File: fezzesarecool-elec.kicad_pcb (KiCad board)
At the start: 2 copper layers, 91 parts, among them J1 Conn_sel, J10 SWD-6, J11 SWD-7, J12 SWD-8, J13 Conn_reset, J14 Conn_LEDs, J15 Audio_input, J16 alim_rpi, J17 alim_audio, J18 alim_led, J2 Conn_start, J3 CAN_conn, J4 CAN_conn, J5 SWD-1, J6 SWD-2, J7 SWD-3, J8 SWD-4, J9 SWD-5, P1 Conn_02x20_Odd_Even, Q1 NMOS-T252, Q2 NMOS-T252, Q3 NMOS-T252, Q4 BSS138, Q5 BSS138, U1 MCP2515-EST, U10 SN74LVC1G00, U11 MC34152, U12 MC34152, U13 LM4991, U2 MCP2551-I-SN, U3 SN74CB3Q3257, U4 SN74CB3Q3257, U5 SN74AC08, U6 SN74CB3Q3257, U7 SN74AC08, U8 SN74CB3Q3257, U9 SN74CB3Q3257, Y1 Crystal_8MHz

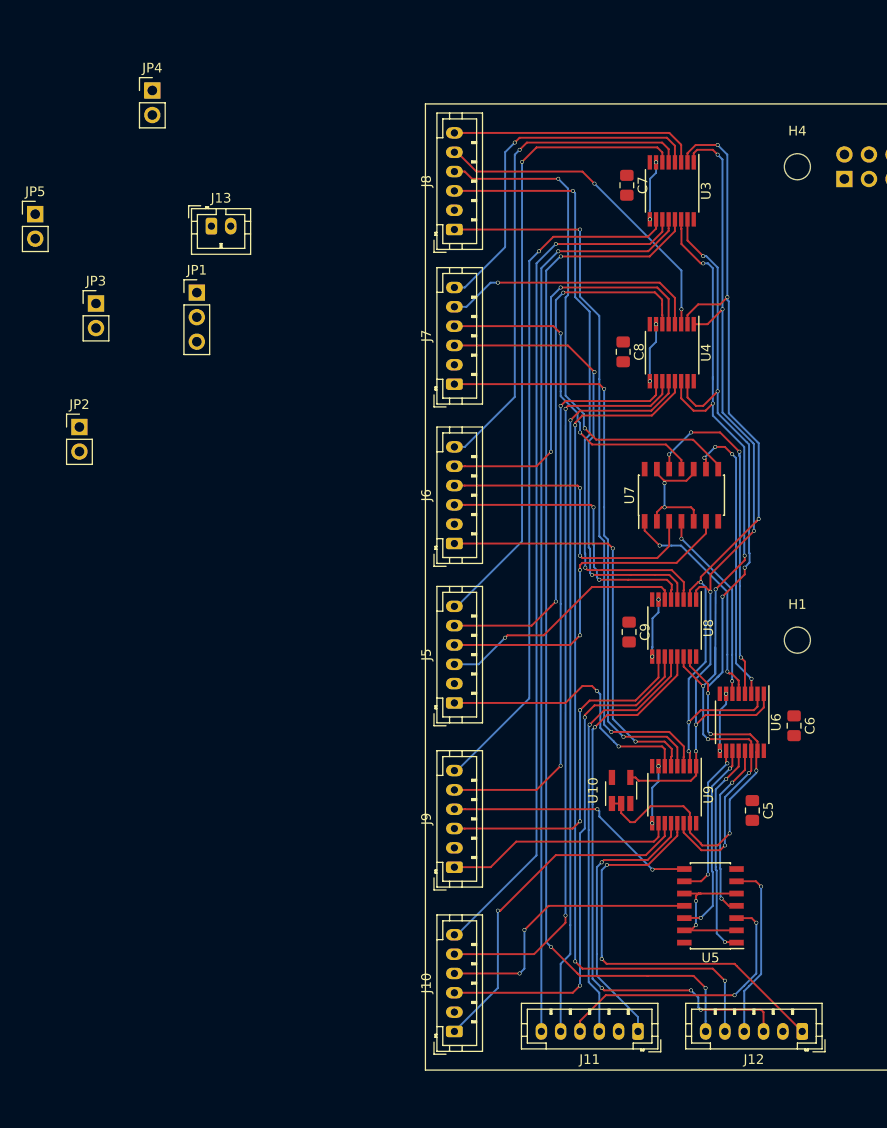
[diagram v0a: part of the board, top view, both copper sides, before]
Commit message: multiplexeur moved
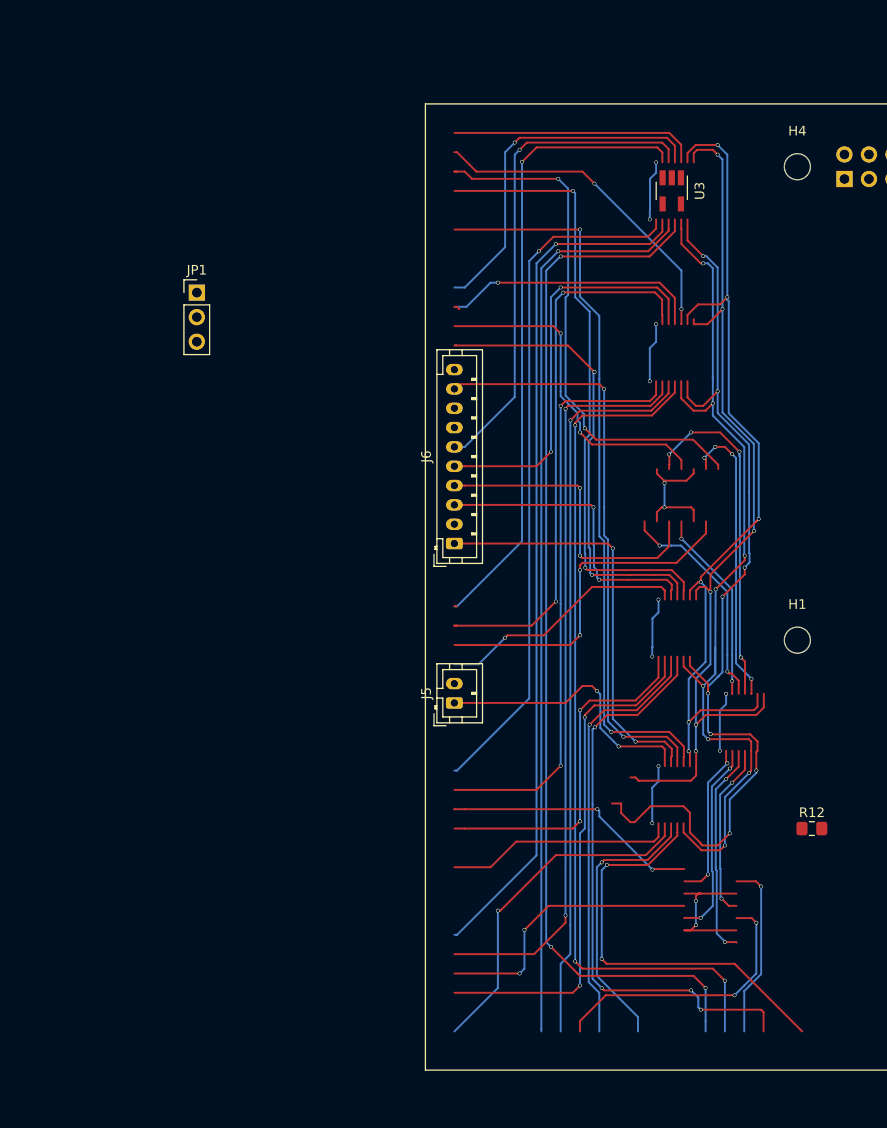
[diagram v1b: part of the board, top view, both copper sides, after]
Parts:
- removed C5, C6, C7, C8, C9: C, Capacitor_SMD:C_0805_2012Metric_Pad1.15x1.40mm_HandSolder
- removed J10: SWD-6, Connector_JST:JST_PH_B6B-PH-K_1x06_P2.00mm_Vertical
- removed J11: SWD-7, Connector_JST:JST_PH_B6B-PH-K_1x06_P2.00mm_Vertical
- removed J12: SWD-8, Connector_JST:JST_PH_B6B-PH-K_1x06_P2.00mm_Vertical
- removed J13: Conn_reset, Connector_JST:JST_PH_B2B-PH-K_1x02_P2.00mm_Vertical
- removed J7: SWD-3, Connector_JST:JST_PH_B6B-PH-K_1x06_P2.00mm_Vertical
- removed J8: SWD-4, Connector_JST:JST_PH_B6B-PH-K_1x06_P2.00mm_Vertical
- removed J9: SWD-5, Connector_JST:JST_PH_B6B-PH-K_1x06_P2.00mm_Vertical
- removed JP2: Jumper_RX, Connector_PinHeader_2.54mm:PinHeader_1x02_P2.54mm_Vertical
- removed JP3: Jumper_TX, Connector_PinHeader_2.54mm:PinHeader_1x02_P2.54mm_Vertical
- removed JP4: Jumper_SWDIO, Connector_PinHeader_2.54mm:PinHeader_1x02_P2.54mm_Vertical
- removed JP5: Jumper_SWCLK, Connector_PinHeader_2.54mm:PinHeader_1x02_P2.54mm_Vertical
- removed U10: SN74LVC1G00, Package_TO_SOT_SMD:SOT-23-5_HandSoldering
- removed U4, U6, U8, U9: SN74CB3Q3257, Package_SO:TSSOP-16_4.4x5mm_P0.65mm
- removed U5, U7: SN74AC08, Package_SO:SOIC-14_3.9x8.7mm_P1.27mm
- added R12: R, Resistor_SMD:R_0805_2012Metric_Pad1.15x1.40mm_HandSolder, F.Cu at (205.0, 166.0)
- J5: value SWD-1 -> Conn_01x02; footprint Connector_JST:JST_PH_B6B-PH-K_1x06_P2.00mm_Vertical -> Connector_JST:JST_PH_B2B-PH-K_1x02_P2.00mm_Vertical
- J6: value SWD-2 -> Conn_01x10; footprint Connector_JST:JST_PH_B6B-PH-K_1x06_P2.00mm_Vertical -> Connector_JST:JST_PH_B10B-PH-K_1x10_P2.00mm_Vertical
- U3: value SN74CB3Q3257 -> SN74AHC1G08; footprint Package_SO:TSSOP-16_4.4x5mm_P0.65mm -> Package_TO_SOT_SMD:SOT-23-5_HandSoldering
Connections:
- J5 pad 1: Net-(J5-Pad1) -> /SWD/GRST
- J6 pad 1: Net-(J6-Pad1) -> +3V3
- J6 pad 2: GND -> Net-(J6-Pad2)
- J6 pad 3: Net-(J6-Pad3) -> /GPIO24(GEN5)
- J6 pad 4: Net-(J6-Pad4) -> /GPIO25(GEN6)
- J6 pad 5: Net-(J6-Pad5) -> /GPIO15(RXD0)
- J6 pad 6: Net-(J6-Pad6) -> /GPIO14(TXD0)
- U3 pad 1: /SWD/~s2 -> /SWD/GRST
- U3 pad 2: /GPIO27(GEN2) -> /SWD/nrst
- U3 pad 3: Net-(J8-Pad6) -> GND
- U3 pad 4: Net-(J7-Pad6) -> Net-(J6-Pad2)
- U3 pad 5: Net-(J6-Pad6) -> +3V3
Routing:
- net Net-(J7-Pad1): track 60.5 -> 0.00 mm, vias 2 -> 0
- net /GPIO22(GEN3): track 102.2 -> 162.7 mm, vias 8 -> 10
- net Net-(J6-Pad6): track 51.8 -> 0.00 mm, vias 1 -> 0
- net /GPIO14(TXD0): track 0.00 -> 51.8 mm, vias 0 -> 1
- net Net-(J6-Pad1): track 43.5 -> 0.00 mm, vias 2 -> 0
- net +3V3: track 0.00 -> 43.5 mm, vias 0 -> 2
- net Net-(J6-Pad5): track 42.6 -> 0.00 mm, vias 2 -> 0
- net /GPIO15(RXD0): track 0.00 -> 42.6 mm, vias 0 -> 2
- net Net-(J6-Pad4): track 32.5 -> 0.00 mm, vias 2 -> 0
- net /GPIO25(GEN6): track 0.00 -> 32.5 mm, vias 0 -> 2
- net Net-(J6-Pad3): track 31.5 -> 0.00 mm, vias 2 -> 0
- net /GPIO24(GEN5): track 0.00 -> 31.5 mm, vias 0 -> 2
- net Net-(J5-Pad1): track 29.0 -> 0.00 mm, vias 2 -> 0
- net /SWD/GRST: track 30.2 -> 59.2 mm, vias 4 -> 6

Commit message: check rpi connexions
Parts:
- removed D3: LED, LED_SMD:LED_0805_2012Metric_Pad1.15x1.40mm_HandSolder
- removed D5: D, Diode_SMD:D_2114_3652Metric_Pad1.85x3.75mm_HandSolder
- removed F2: Fuse, Fuse:Fuse_1206_3216Metric_Pad1.42x1.75mm_HandSolder
- removed J16: alim_rpi, Connector_Phoenix_MSTB:PhoenixContact_MSTBA_2,5_2-G_1x02_P5.00mm_Horizontal
- removed J17: alim_audio, Connector_Phoenix_MSTB:PhoenixContact_MSTBA_2,5_2-G_1x02_P5.00mm_Horizontal
- removed JP6: Jumper_NC_Dual, Jumper:SolderJumper-3_P1.3mm_Open_RoundedPad1.0x1.5mm_NumberLabels
- removed R14, R15: R, Resistor_SMD:R_0805_2012Metric_Pad1.15x1.40mm_HandSolder
- added J7: alim_5V, Connector_Phoenix_MSTB:PhoenixContact_MSTBA_2,5_2-G_1x02_P5.00mm_Horizontal, F.Cu at (224.0, 141.0)
- added R13: R, Resistor_SMD:R_0805_2012Metric_Pad1.15x1.40mm_HandSolder, B.Cu at (222.5, 137.5)
- C14, D6, F3, R10, R11, R12, R16, U13, U3: moved to B.Cu
- J18: value alim_led -> alim_jacky
- J3, J4: footprint Connector_JST:JST_XH_B04B-XH-A_1x04_P2.50mm_Vertical -> Connector_JST:JST_XH_B05B-XH-A_1x05_P2.50mm_Vertical
- moved R16 159.1 mm to (205.0, 138.5), turned to 90 degrees
- moved D4 150.7 mm to (202.5, 138.5), turned to 90 degrees
- moved D6 144.0 mm to (213.5, 146.0)
- moved F3 136.0 mm to (207.5, 141.5), turned to 270 degrees
- moved J18 133.5 mm to (211.0, 141.0)
- moved JP7 127.1 mm to (209.7, 136.0)
- moved J2 122.0 mm to (253.4, 104.9)
- moved J1 122.0 mm to (245.5, 104.9)
- moved F1 111.5 mm to (221.0, 141.5), turned to 270 degrees
- moved D2 110.8 mm to (224.5, 146.5), turned to 0 degrees
- moved D1 108.0 mm to (217.5, 137.0), turned to 0 degrees
- moved R1 103.7 mm to (246.5, 110.0)
- moved R2 93.8 mm to (252.0, 110.0), turned to 180 degrees
- moved LS1 87.9 mm to (229.5, 129.0)
- moved JP1 83.7 mm to (224.0, 123.5), turned to 90 degrees
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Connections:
- C16 pad 1: +5VL -> +5VD
- J3 pad 3: Net-(J3-Pad3) -> /SWD/GRST
- J3 pad 4: +7.5V -> Net-(J3-Pad4)
- J4 pad 3: Net-(J3-Pad3) -> /SWD/GRST
- J4 pad 4: +7.5V -> Net-(J3-Pad4)
- U13 pad 6: +5VL -> +5VD
- U2 pad 7: Net-(J3-Pad3) -> Net-(J3-Pad4)
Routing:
- net /GPIO22(GEN3): track 162.7 -> 0.00 mm, vias 10 -> 0
- net Net-(J12-Pad6): track 108.7 -> 0.00 mm, vias 3 -> 0
- net /SWD/~s2: track 95.4 -> 0.00 mm, vias 6 -> 0
- net Net-(J11-Pad6): track 95.0 -> 0.00 mm, vias 1 -> 0
- net /GPIO17(GEN0): track 94.4 -> 0.00 mm, vias 8 -> 0
- net /GPIO27(GEN2): track 91.3 -> 0.00 mm, vias 6 -> 0
- net Net-(J12-Pad5): track 90.1 -> 0.00 mm, vias 3 -> 0
- net Net-(J10-Pad6): track 88.8 -> 0.00 mm, vias 1 -> 0
- net Net-(J10-Pad5): track 78.1 -> 0.00 mm, vias 2 -> 0
- net Net-(J8-Pad1): track 76.5 -> 0.00 mm, vias 2 -> 0
- net Net-(J11-Pad5): track 76.3 -> 0.00 mm, vias 1 -> 0
- net Net-(J9-Pad6): track 71.6 -> 0.00 mm, vias 1 -> 0
- net Net-(J5-Pad6): track 65.7 -> 0.00 mm, vias 1 -> 0
- net Net-(J8-Pad3): track 64.8 -> 0.00 mm, vias 2 -> 0
- net Net-(J9-Pad5): track 61.1 -> 0.00 mm, vias 2 -> 0
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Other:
- board outline added: 65 x 56 mm

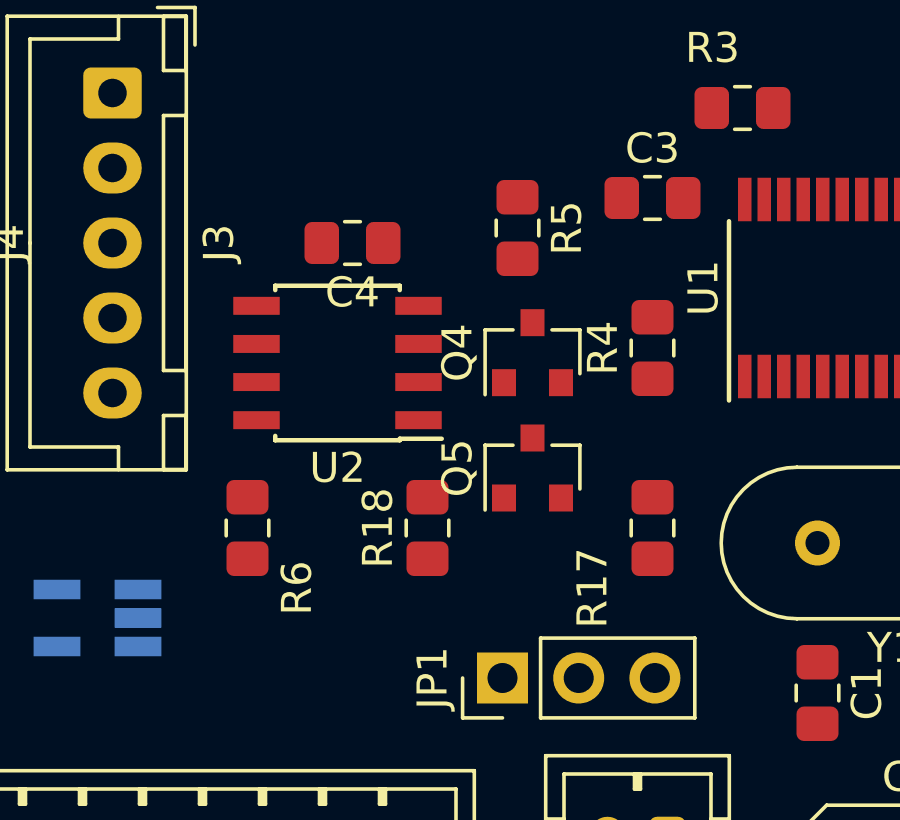
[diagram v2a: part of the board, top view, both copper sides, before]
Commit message: CAN transiver changed, redy to route
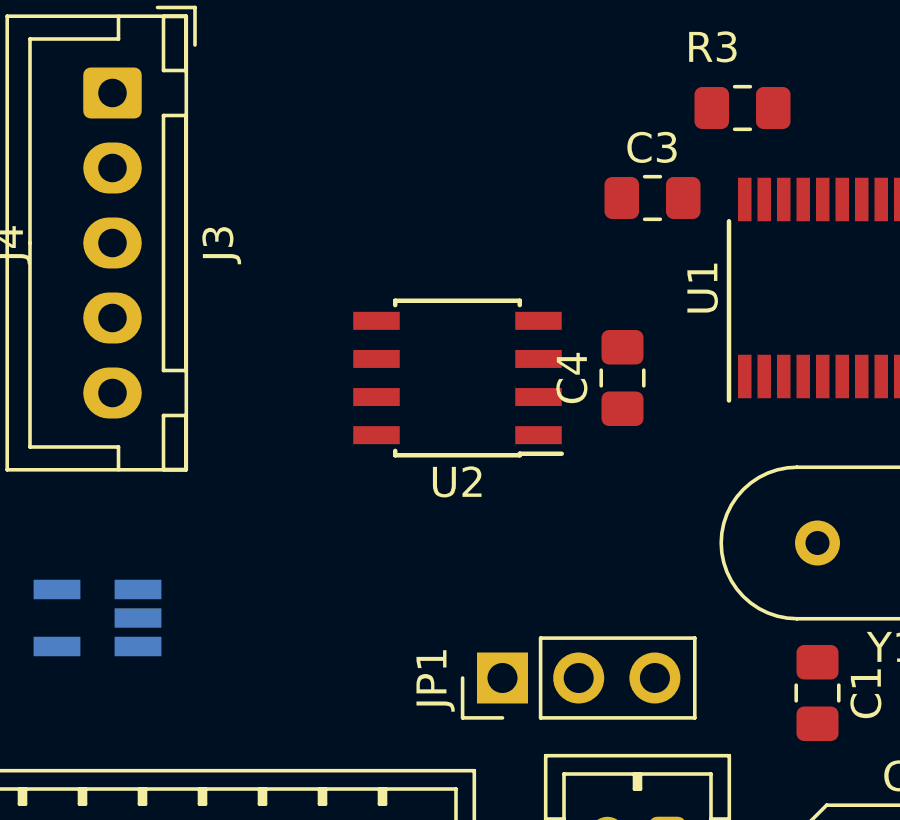
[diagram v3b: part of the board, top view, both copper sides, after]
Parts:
- removed Q4, Q5: BSS138, Package_TO_SOT_SMD:SOT-23
- removed R17, R18, R4, R5, R6: R, Resistor_SMD:R_0805_2012Metric_Pad1.15x1.40mm_HandSolder
- U2: value MCP2551-I-SN -> TCAN332
- moved C4 10.1 mm to (228.0, 113.5), turned to 90 degrees
- moved U2 4.03 mm to (222.5, 113.5)
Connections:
- C4 pad 2: +5V -> +3V3
- U1 pad 1: Net-(Q5-Pad2) -> Net-(U1-Pad1)
- U1 pad 2: Net-(Q4-Pad2) -> Net-(U1-Pad2)
- U2 pad 1: Net-(Q5-Pad3) -> Net-(U1-Pad1)
- U2 pad 3: +5V -> +3V3
- U2 pad 4: Net-(Q4-Pad3) -> Net-(U1-Pad2)

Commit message: routed
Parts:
- added R4: R, Resistor_SMD:R_0805_2012Metric_Pad1.15x1.40mm_HandSolder, F.Cu at (248.3, 103.6)
- added R5: R, Resistor_SMD:R_0805_2012Metric_Pad1.15x1.40mm_HandSolder, F.Cu at (257.4, 103.4)
- C3: moved to B.Cu
- moved JP7 21.6 mm to (225.3, 121.0), turned to 90 degrees
- moved R13 20.6 mm to (201.9, 137.0), turned to 270 degrees
- moved D1 16.1 mm to (201.9, 141.0), turned to 90 degrees
- moved JP1 7.00 mm to (217.0, 123.5), turned to 180 degrees
- moved C3 6.53 mm to (234.9, 110.2), turned to 180 degrees
- moved R2 4.19 mm to (255.9, 111.5)
- moved C4 3.02 mm to (226.9, 110.7)
- moved U2 3.02 mm to (221.4, 110.7)
- moved J1 2.70 mm to (247.3, 107.0)
- moved J6 2.50 mm to (221.0, 132.0)
- moved J2 2.47 mm to (254.8, 107.0)
- moved R16 2.39 mm to (205.5, 136.2), turned to 180 degrees
- moved D4 2.36 mm to (204.4, 139.8)
- moved R1 2.35 mm to (248.3, 111.5), turned to 180 degrees
- moved R8 1.98 mm to (263.5, 133.2), turned to 90 degrees
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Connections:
- J1 pad 1: /GPIO6 -> GND
- J1 pad 2: GND -> Net-(J1-Pad2)
- J18 pad 1: Net-(F3-Pad1) -> GND
- J18 pad 2: GND -> Net-(F3-Pad1)
- J2 pad 1: /GPIO26 -> GND
- J2 pad 2: GND -> Net-(J2-Pad2)
- J7 pad 1: Net-(F1-Pad1) -> GND
- J7 pad 2: GND -> Net-(F1-Pad1)
- R1 pad 1: /GPIO6 -> Net-(J1-Pad2)
- R2 pad 1: /GPIO26 -> Net-(J2-Pad2)
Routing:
- net GND: track 0.00 -> 260.0 mm, vias 0 -> 18
- net +3V3: track 0.00 -> 141.7 mm, vias 0 -> 8
- net +5V: track 0.00 -> 98.8 mm, vias 0 -> 4
- net +5VD: track 0.00 -> 93.6 mm, vias 0 -> 6
- net +7.5V: track 0.00 -> 86.6 mm, vias 0 -> 3
- net /SWD/GRST: track 0.00 -> 66.3 mm, vias 0 -> 2
- net /GPIO12(PWM0): track 0.00 -> 58.7 mm, vias 0 -> 1
- net /GPIO16: track 0.00 -> 53.7 mm, vias 0 -> 4
- net /GPIO22(GEN3): track 0.00 -> 49.9 mm, vias 0 -> 2
- net /GPIO25(GEN6): track 0.00 -> 48.4 mm, vias 0 -> 4
- net /GPIO27(GEN2): track 0.00 -> 47.0 mm, vias 0 -> 2
- net Net-(D6-Pad1): track 0.00 -> 44.9 mm, vias 0 -> 3
- net /GPIO24(GEN5): track 0.00 -> 44.2 mm, vias 0 -> 2
- net /GPIO17(GEN0): track 0.00 -> 43.4 mm, vias 0 -> 2
- net /GPIO19(SPI1_MISO): track 0.00 -> 41.6 mm, vias 0 -> 4
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- added copper zone on B.Cu, net GND
- added copper zone on F.Cu, net GND

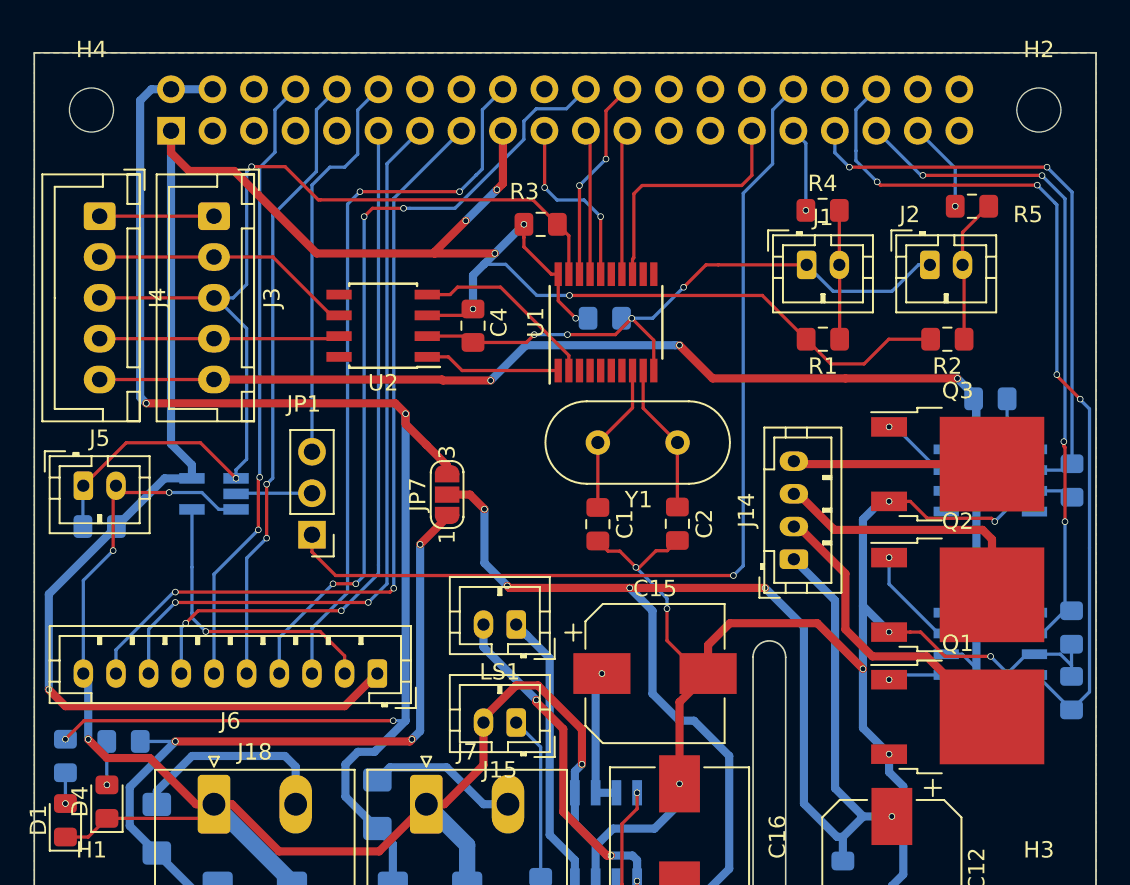
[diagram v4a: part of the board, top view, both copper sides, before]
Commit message: resistors addes
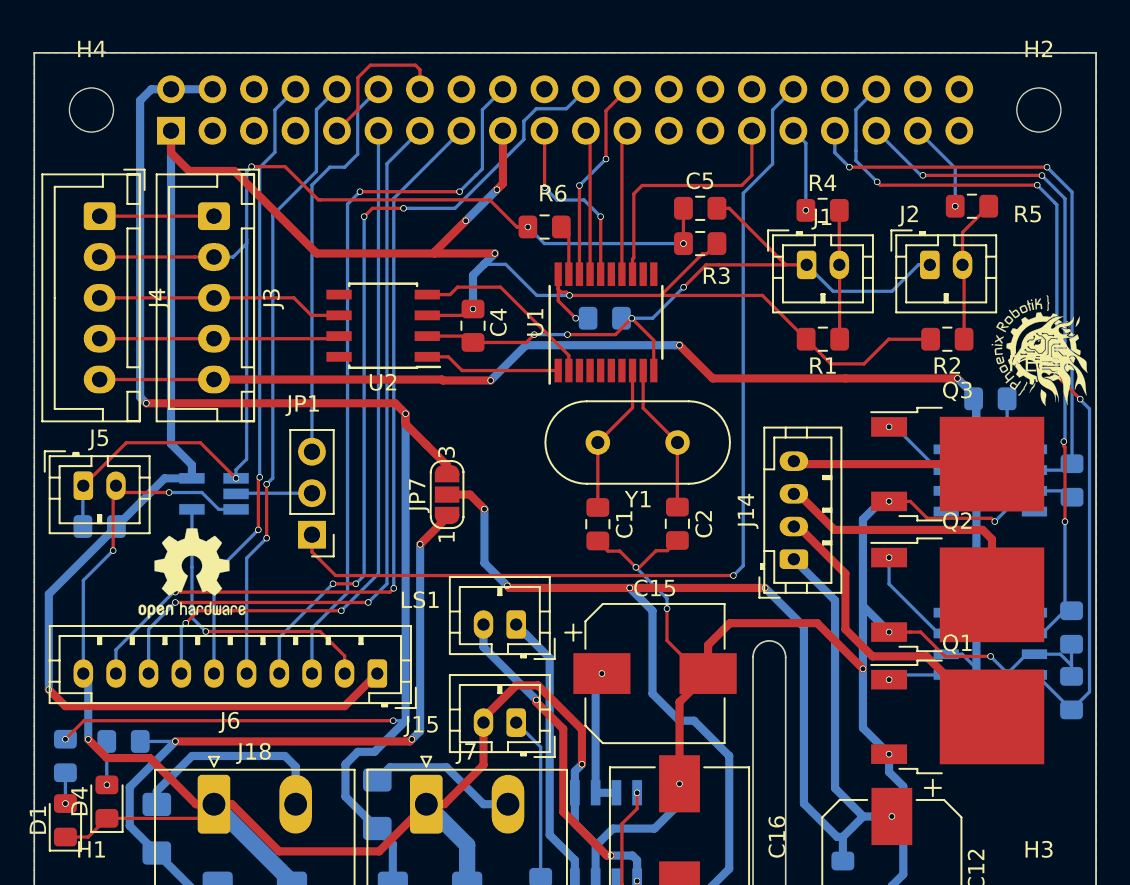
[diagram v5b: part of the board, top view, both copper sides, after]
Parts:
- added C5: C, Capacitor_SMD:C_0805_2012Metric_Pad1.15x1.40mm_HandSolder, F.Cu at (240.8, 103.5)
- added R6: R, Resistor_SMD:R_0805_2012Metric_Pad1.15x1.40mm_HandSolder, F.Cu at (231.2, 104.7)
- added REF**: OSHW-Logo2_7.3x6mm_SilkScreen, Symbol:OSHW-Logo2_7.3x6mm_SilkScreen, F.Cu at (209.7, 125.9)
- added REF**: Logo_8,5mm, PhoenixRobotik:Logo_8,5mm, F.Cu at (261.6, 113.0)
- moved R3 9.84 mm to (240.8, 105.7), turned to 0 degrees
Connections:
- J3 pad 2: Net-(J3-Pad2) -> /SWD/GRST
- J3 pad 3: /SWD/GRST -> Net-(J3-Pad3)
- J4 pad 2: Net-(J3-Pad2) -> /SWD/GRST
- J4 pad 3: /SWD/GRST -> Net-(J3-Pad3)
- P1 pad 16: /GPIO23(GEN4) -> (no net)
- P1 pad 26: /GPIO7(SPI1_CE_N) -> (no net)
- P1 pad 27: /ID_SD -> (no net)
- P1 pad 28: /ID_SC -> (no net)
- P1 pad 3: /GPIO2(SDA1) -> (no net)
- P1 pad 38: /GPIO20(SPI1_MOSI) -> (no net)
- P1 pad 40: /GPIO21(SPI1_SCK) -> (no net)
- P1 pad 5: /GPIO3(SCL1) -> (no net)
- P1 pad 7: /GPIO4(GCLK) -> (no net)
- U1 pad 11: Net-(U1-Pad11) -> (no net)
- U1 pad 12: Net-(U1-Pad12) -> (no net)
- U1 pad 15: Net-(U1-Pad15) -> (no net)
- U1 pad 19: /SWD/GRST -> Net-(R6-Pad1)
- U1 pad 3: Net-(U1-Pad3) -> (no net)
- U1 pad 4: Net-(U1-Pad4) -> (no net)
- U1 pad 5: Net-(U1-Pad5) -> (no net)
- U1 pad 6: Net-(U1-Pad6) -> (no net)
- U1 pad 7: Net-(U1-Pad7) -> (no net)
- U11 pad 1: Net-(U11-Pad1) -> (no net)
- U11 pad 8: Net-(U11-Pad8) -> (no net)
- U12 pad 1: Net-(U12-Pad1) -> (no net)
- U12 pad 5: Net-(U12-Pad5) -> (no net)
- U12 pad 8: Net-(U12-Pad8) -> (no net)
- U2 pad 5: Net-(U2-Pad5) -> (no net)
- U2 pad 6: Net-(J3-Pad2) -> Net-(J3-Pad3)
- U2 pad 8: Net-(U2-Pad8) -> (no net)
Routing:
- net Net-(J3-Pad2): track 16.1 -> 0.00 mm
- net Net-(J3-Pad3): track 0.00 -> 15.7 mm
- net GND: track 260.0 -> 274.9 mm
- net /SWD/GRST: track 66.3 -> 73.5 mm, vias 2 -> 4
- net Net-(R6-Pad1): track 0.00 -> 3.08 mm
- net +3V3: track 141.7 -> 141.5 mm, vias 8 -> 7
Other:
- rule trace_min: 0.1525 -> 0.2
